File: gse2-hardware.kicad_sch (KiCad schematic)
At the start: 66 parts, among them J1 PJ-002A, J16 ARM, J17 ALARM, J2 PJ-002A, J3 ARM Cortex Debug, J33 AI_Ports, J34 Misc_Ports, J4 USB-C, Q1 DMP3099L, Q15 DMG3402L, U27 USBLC6-2SC6, Y1 16MHz

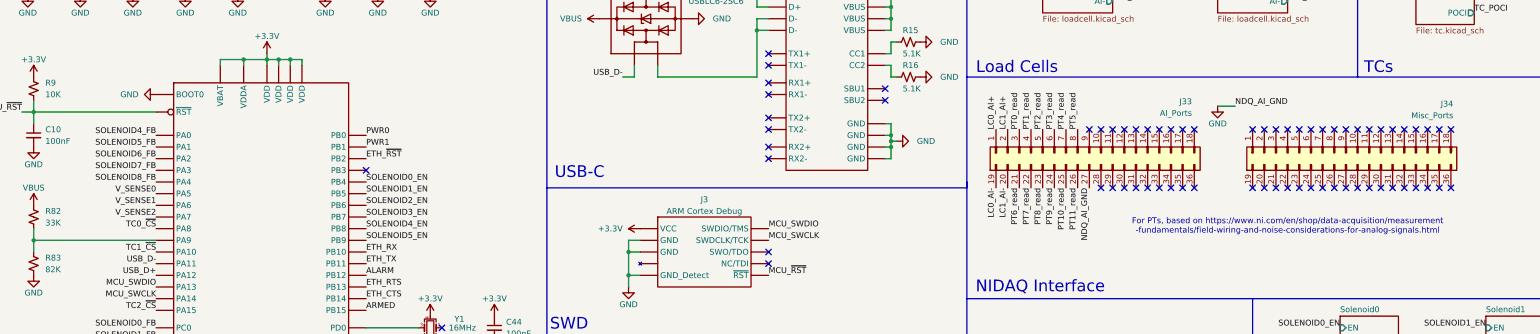
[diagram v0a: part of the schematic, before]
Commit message: Layed out (no edge cuts)g
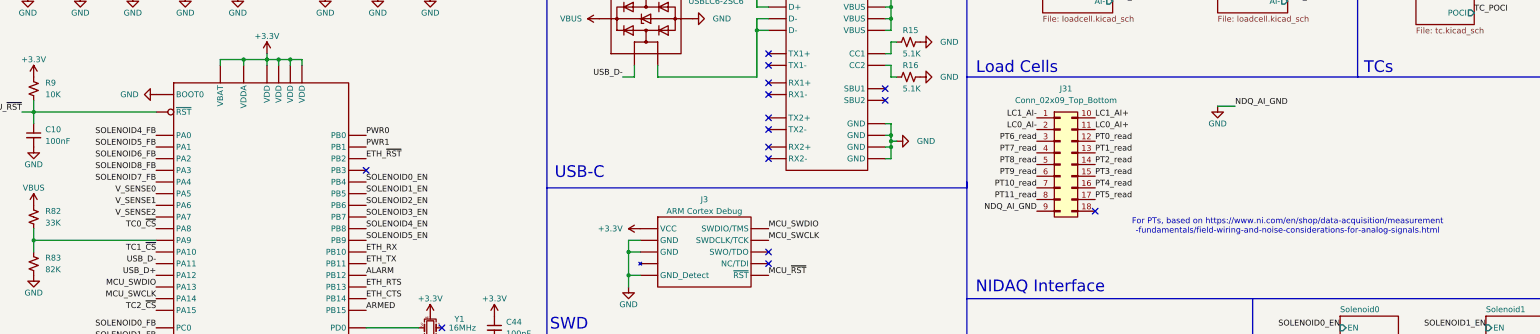
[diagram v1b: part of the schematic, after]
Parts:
- removed J33: AI_Ports, symbol Connector_Generic:Conn_02x18_Top_Bottom
- removed J34: Misc_Ports, symbol Connector_Generic:Conn_02x18_Top_Bottom
- added J31: Conn_02x09_Top_Bottom, 0UCIRP-KiCAD-Lib:2x9_MOLEX, symbol Connector_Generic:Conn_02x09_Top_Bottom
- J17: footprint TerminalBlock_MetzConnect:TerminalBlock_MetzConnect_Type055_RT01502HDWU_1x02_P5.00mm_Horizontal -> 0UCIRP-KiCAD-Lib:GX-16 2 pin
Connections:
- net GND: now also J31.9 (Pin_9)
- net LC0_AI+: now also J31.11 (Pin_11)
- net LC0_AI-: now also J31.2 (Pin_2)
- net LC1_AI+: now also J31.10 (Pin_10)
- net LC1_AI-: now also J31.1 (Pin_1)
- net PT0_read: now also J31.12 (Pin_12)
- net PT10_read: now also J31.7 (Pin_7)
- net PT11_read: now also J31.8 (Pin_8)
- net PT1_read: now also J31.13 (Pin_13)
- net PT2_read: now also J31.14 (Pin_14)
- net PT3_read: now also J31.15 (Pin_15)
- net PT4_read: now also J31.16 (Pin_16)
- net PT5_read: now also J31.17 (Pin_17)
- net PT6_read: now also J31.3 (Pin_3)
- net PT7_read: now also J31.4 (Pin_4)
- net PT8_read: now also J31.5 (Pin_5)
- net PT9_read: now also J31.6 (Pin_6)
- net SOLENOID7_FB: now also U2.20 (PA4); no longer U2.17 (PA3)
- net SOLENOID8_FB: now also U2.17 (PA3); no longer U2.20 (PA4)
- no-connect marks 73 -> 19

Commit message: Fixed updates form last night not pushing
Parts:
- added H1, H2, H3, H4: MountingHole_Pad, MountingHole:MountingHole_4.3mm_M4_Pad_Via, symbol Mechanical:MountingHole_Pad
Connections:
- net at D1.2 (A), J1.1, R2.2: now also R10.2
- net at D4.2 (A), J2.1, R7.2: now also R8.2
- net at D1.1 (K), D4.1 (K), F1.1: no longer R10.2, R8.2
- no-connect marks 19 -> 23
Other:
- moved on the sheet: D1, D4, D5, D6, R10, R8

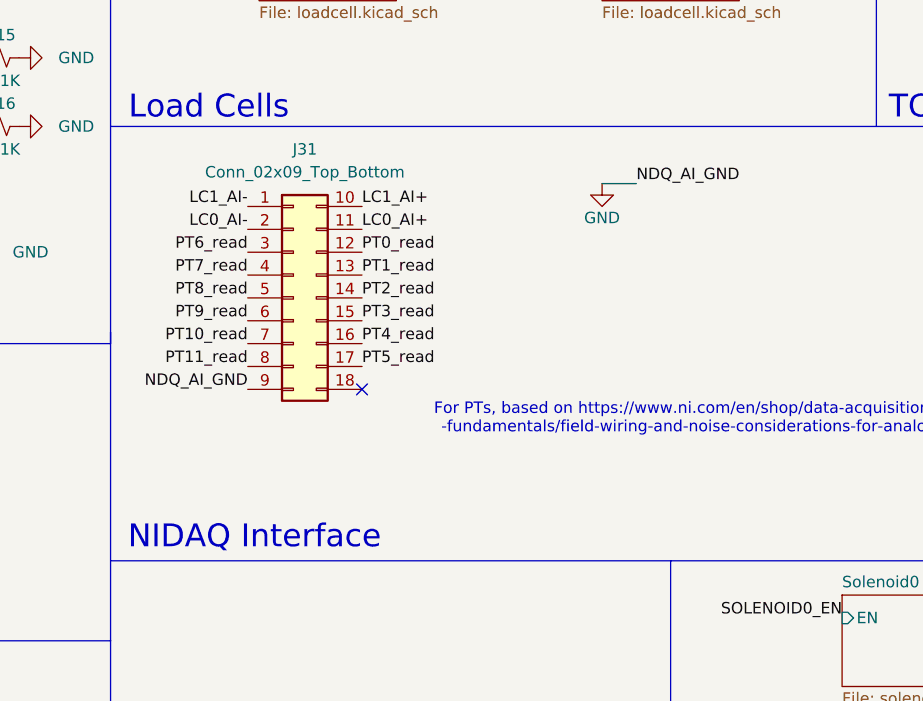
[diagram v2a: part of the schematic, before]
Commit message: Fixed connectors
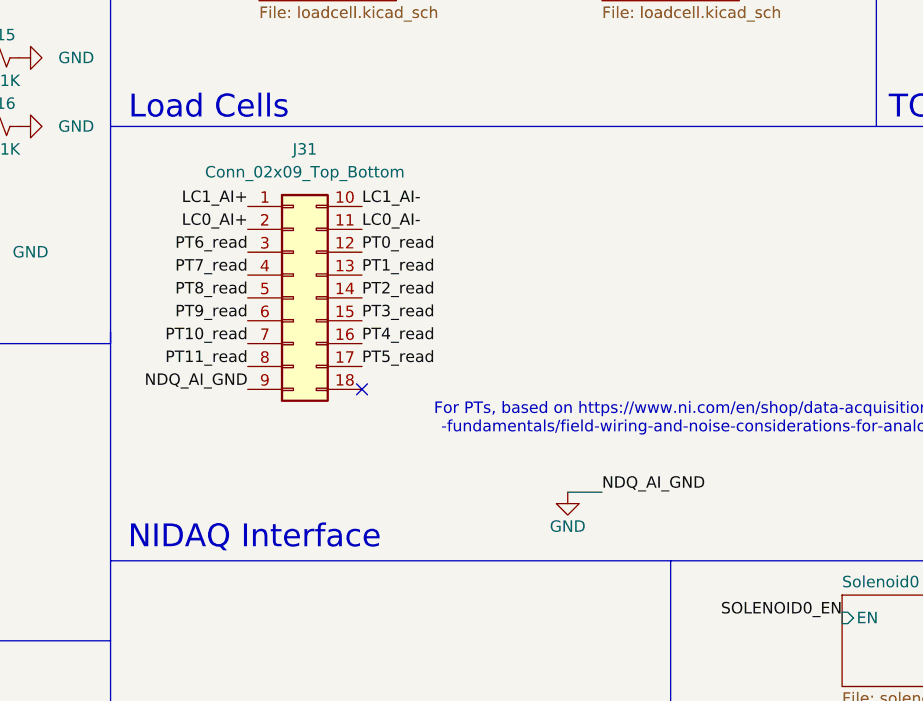
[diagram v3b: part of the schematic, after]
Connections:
- net LC0_AI+: now also J31.2 (Pin_2); no longer J31.11 (Pin_11)
- net LC0_AI-: now also J31.11 (Pin_11); no longer J31.2 (Pin_2)
- net LC1_AI+: now also J31.1 (Pin_1); no longer J31.10 (Pin_10)
- net LC1_AI-: now also J31.10 (Pin_10); no longer J31.1 (Pin_1)
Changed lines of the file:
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@@
 	(wire
 		(pts
-			(xy 287.02 48.26) (xy 290.83 48.26)
+			(xy 283.21 82.55) (xy 287.02 82.55)
 		)
 		(stroke
@@
 		)
 	)
+	(label "LC0_AI+"
+		(at 247.65 53.34 180)
+		(effects
+			(font
+				(size 1.27 1.27)
+			)
+			(justify right bottom)
+		)
+	)
 	(label "SOLENOID0_FB"
 		(at 326.39 101.6 0)
@@
 		)
 	)
-	(label "LC0_AI-"
-		(at 247.65 53.34 180)
-		(effects
-			(font
-				(size 1.27 1.27)
-			)
-			(justify right bottom)
-		)
-	)
 	(label "MCU_SWCLK"
 		(at 189.23 77.47 0)
@@
 		)
 	)
+	(label "LC0_AI-"
+		(at 260.35 53.34 0)
+		(effects
+			(font
+				(size 1.27 1.27)
+			)
+			(justify left bottom)
+		)
+	)
 	(label "EMATCH1_FIRE"
 		(at 55.88 116.84 180)
@@
 		)
 	)
+	(label "LC1_AI-"
+		(at 260.35 50.8 0)
+		(effects
+			(font
+				(size 1.27 1.27)
+			)
+			(justify left bottom)
+		)
+	)
 	(label "SOLENOID4_EN"
 		(at 101.6 74.93 0)
@@
 	)
 	(label "NDQ_AI_GND"
-		(at 290.83 48.26 0)
+		(at 287.02 82.55 0)
 		(effects
 			(font
@@
 		)
 	)
+	(label "LC1_AI+"
+		(at 247.65 50.8 180)
+		(effects
+			(font
+				(size 1.27 1.27)
+			)
+			(justify right bottom)
+		)
+	)
 	(label "TC_SCK"
 		(at 358.14 24.13 180)
@@
 		)
 	)
-	(label "LC1_AI-"
-		(at 247.65 50.8 180)
-		(effects
-			(font
-				(size 1.27 1.27)
-			)
-			(justify right bottom)
-		)
-	)
 	(label "SOLENOID5_FB"
 		(at 55.88 57.15 180)
@@
 		)
 	)
-	(label "LC0_AI+"
-		(at 260.35 53.34 0)
-		(effects
-			(font
-				(size 1.27 1.27)
-			)
-			(justify left bottom)
-		)
-	)
 	(label "PT0_read"
 		(at 26.67 161.29 0)
@@
 		)
 	)
-	(label "LC1_AI+"
-		(at 260.35 50.8 0)
-		(effects
-			(font
-				(size 1.27 1.27)
-			)
-			(justify left bottom)
-		)
-	)
 	(label "PT0_read"
 		(at 260.35 55.88 0)
@@
 	(symbol
 		(lib_id "power:GND")
-		(at 287.02 48.26 0)
+		(at 283.21 82.55 0)
 		(unit 1)
 		(exclude_from_sim no)
@@
 		(dnp no)
 		(property "Reference" "#PWR03"
-			(at 287.02 54.61 0)
+			(at 283.21 88.9 0)
 			(effects
 				(font
@@
 		)
 		(property "Value" "GND"
-			(at 287.02 52.07 0)
+			(at 283.21 86.36 0)
 			(effects
 				(font
@@
 		)
 		(property "Footprint" ""
-			(at 287.02 48.26 0)
+			(at 283.21 82.55 0)
 			(effects
 				(font
@@
 		)
 		(property "Datasheet" ""
-			(at 287.02 48.26 0)
+			(at 283.21 82.55 0)
 			(effects
 				(font
@@
 		)
 		(property "Description" ""
-			(at 287.02 48.26 0)
+			(at 283.21 82.55 0)
 			(effects
 				(font

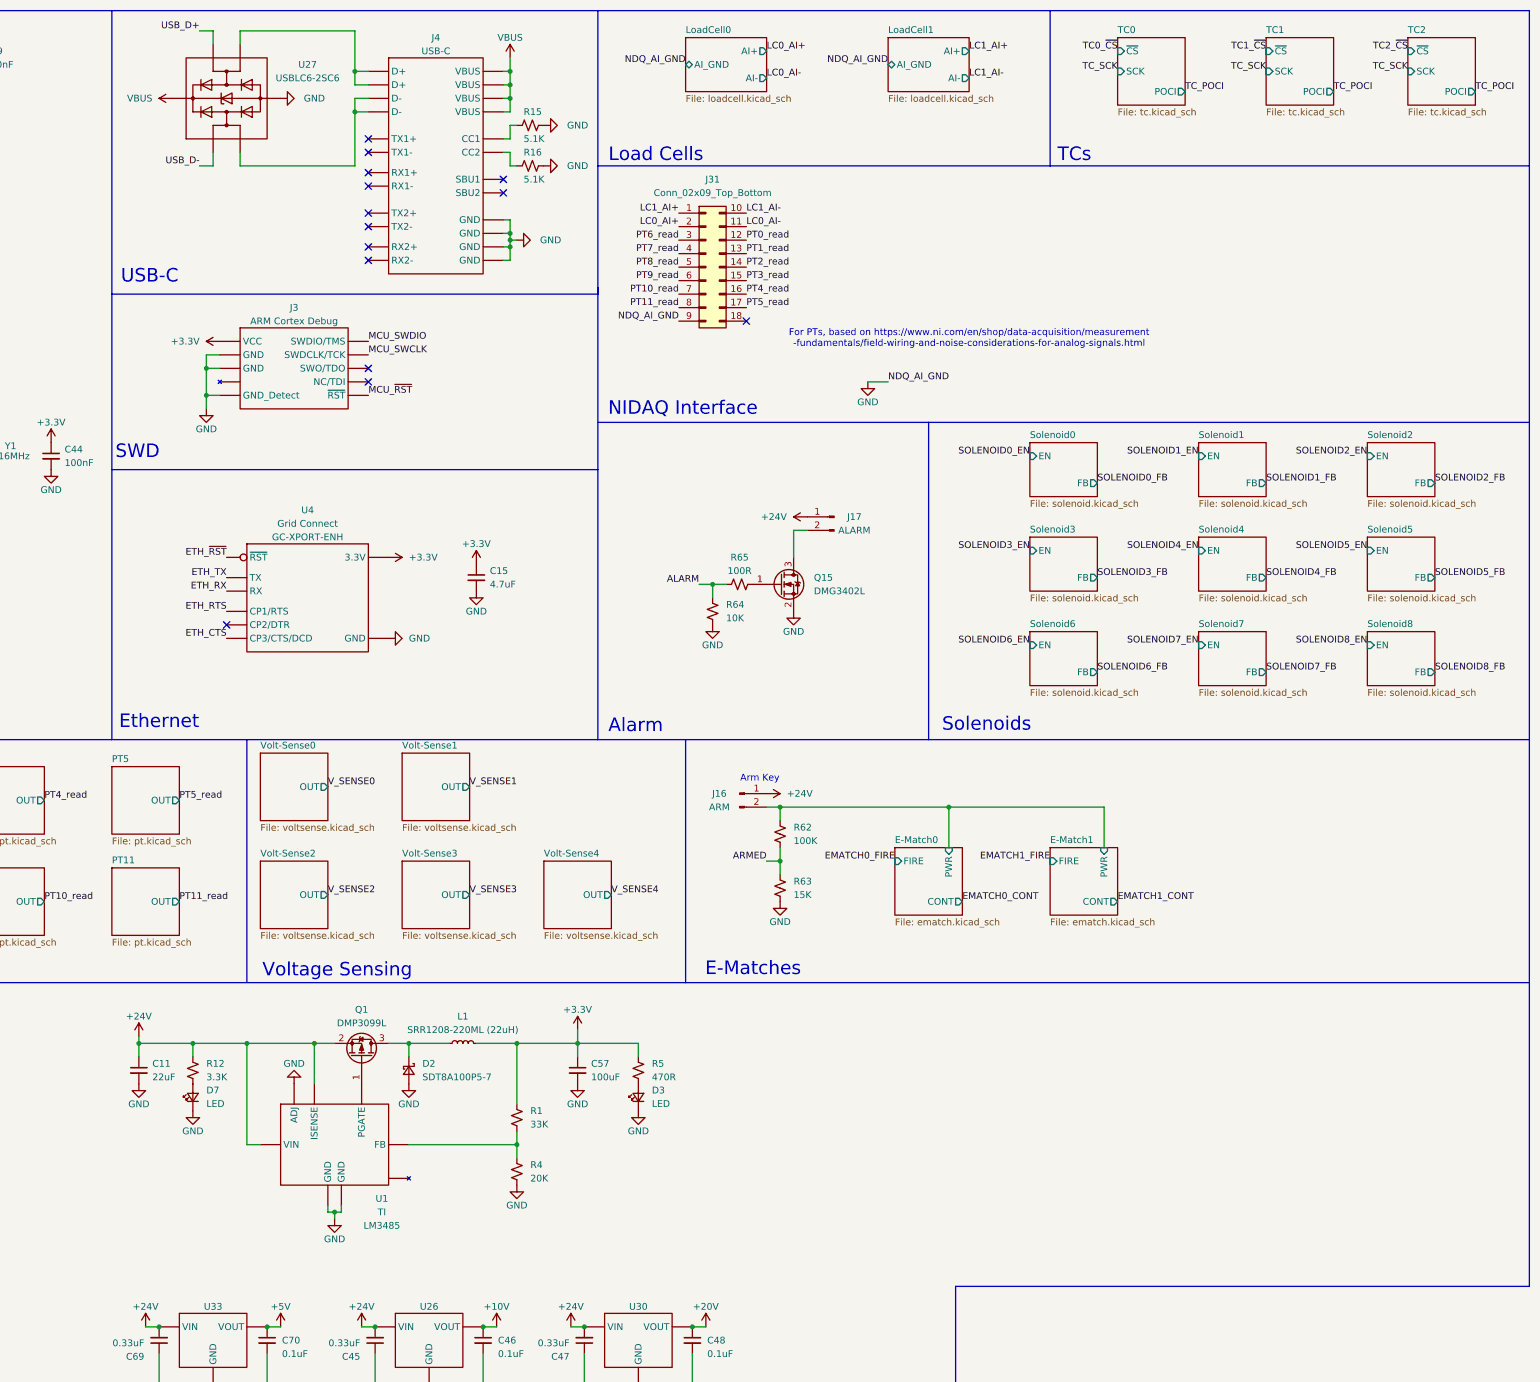
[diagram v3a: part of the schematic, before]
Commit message: Ready to order besides BOM. I might mess w/ silkscreen more. 3v3 reg changed
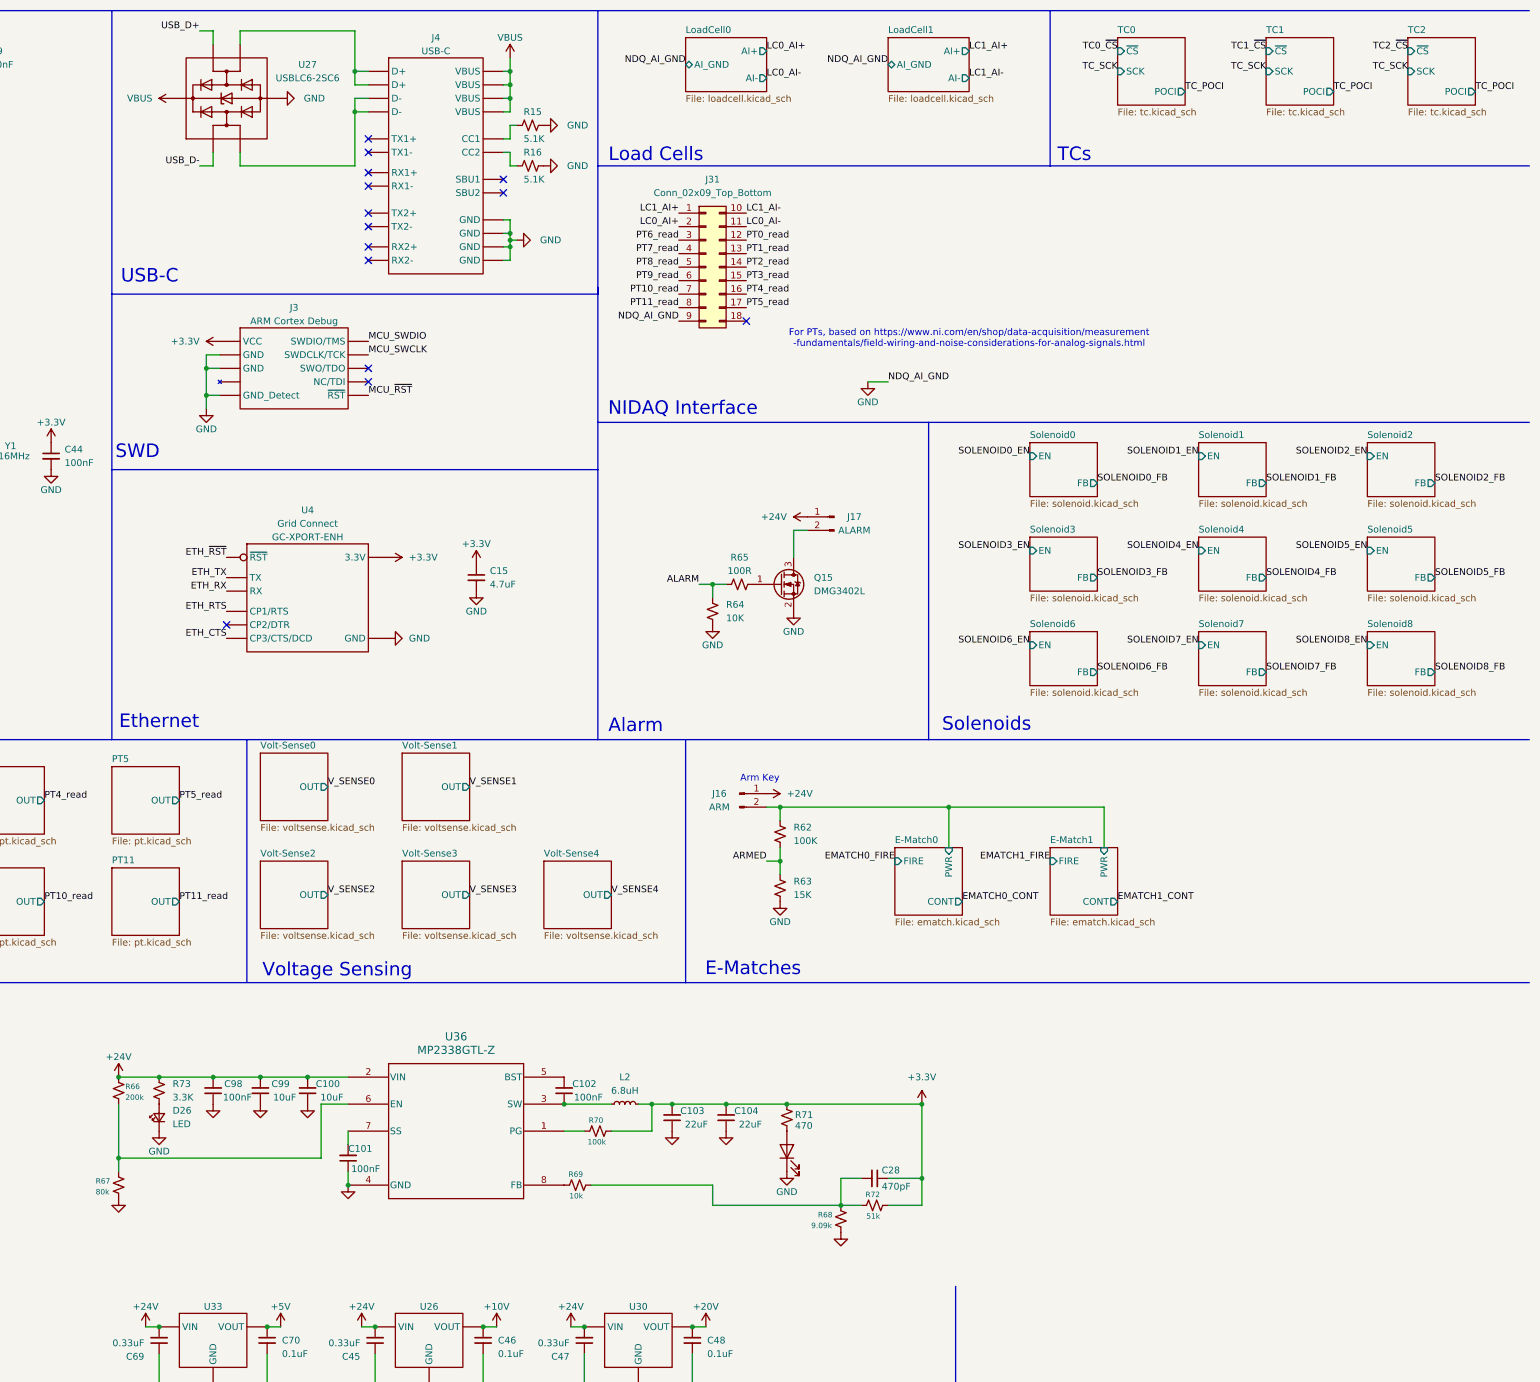
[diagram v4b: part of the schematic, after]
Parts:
- removed C11: 22uF, Capacitor_SMD:C_0603_1608Metric, symbol Device:C_Small
- removed C57: 100uF, Capacitor_SMD:C_0603_1608Metric, symbol Device:C_Small
- removed D2: SDT8A100P5-7, Diode_SMD:D_PowerDI-5, symbol Device:D_Schottky_Small
- removed D3, D7: LED, LED_SMD:LED_0603_1608Metric, symbol Device:LED_Small
- removed L1: SRR1208-220ML (22uH), Inductor_SMD:L_Bourns_SRR1208_12.7x12.7mm, symbol Device:L_Small
- removed Q1: DMP3099L, Package_TO_SOT_SMD:SOT-23-3, symbol Device:Q_PMOS_GSD
- removed R1: 33K, Resistor_SMD:R_0603_1608Metric, symbol Device:R_Small_US
- removed R12: 3.3K, Resistor_SMD:R_0603_1608Metric, symbol Device:R_Small_US
- removed R4: 20K, Resistor_SMD:R_0603_1608Metric, symbol Device:R_Small_US
- removed R5: 470R, Resistor_SMD:R_0603_1608Metric, symbol Device:R_Small_US
- removed U1: ~, Package_SO:VSSOP-8_3x3mm_P0.65mm, symbol UCIRP-KiCAD-Lib:LM3485
- added C100, C99: 10uF, Capacitor_SMD:C_0603_1608Metric, symbol Device:C_Small
- added C101, C102, C98: 100nF, Capacitor_SMD:C_0603_1608Metric, symbol Device:C_Small
- added C103, C104: 22uF, Capacitor_SMD:C_0603_1608Metric, symbol Device:C_Small
- added C28: 470pF, Capacitor_SMD:C_0603_1608Metric, symbol Device:C_Small
- added D26: LED, LED_SMD:LED_0603_1608Metric, symbol Device:LED_Small
- added D42: BLUE_LED, Diode_SMD:D_0603_1608Metric, symbol Device:LED
- added L2: 6.8uH, 0UCIRP-KiCAD-Lib:IND_VLS6045EX-6R8M, symbol Device:L_Small
- added R66: 200k, Resistor_SMD:R_0603_1608Metric, symbol Device:R_Small_US
- added R67: 80k, Resistor_SMD:R_0603_1608Metric, symbol Device:R_Small_US
- added R68: 9.09k, Resistor_SMD:R_0603_1608Metric, symbol Device:R_Small_US
- added R69: 10k, Resistor_SMD:R_0603_1608Metric, symbol Device:R_Small_US
- added R70: 100k, Resistor_SMD:R_0603_1608Metric, symbol Device:R_Small_US
- added R71: 470, Resistor_SMD:R_0603_1608Metric, symbol Device:R_Small_US
- added R72: 51k, Resistor_SMD:R_0603_1608Metric, symbol Device:R_Small_US
- added R73: 3.3K, Resistor_SMD:R_0603_1608Metric, symbol Device:R_Small_US
- added U36: MP2338GTL-Z, SOT583_MP2338_MNP, symbol UCIRP-KiCAD-Lib:MP2338GTL-Z
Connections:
- net +24V: now also C100.2, C98.2, C99.2, R66.1, R73.2, U36.2 (VIN)
- net +3.3V: now also C103.2, C104.2, C28.1, L2.2, R70.2, R71.1, R72.2
- net GND: now also C100.1, C101.1, C103.1, C104.1, C98.1, C99.1, D26.1 (K), D42.1 (K), R67.2, R68.2, U36.4 (GND)
- new net: C28.2, R68.1, R69.2, R72.1
- new net: R69.1, U36.8 (FB)
- new net: C101.2, U36.7 (SS)
- new net: D26.2 (A), R73.1
- new net: R66.2, R67.1, U36.6 (EN)
- new net: R70.1, U36.1 (PG)
- new net: C102.1, L2.1, U36.3 (SW)
- new net: C102.2, U36.5 (BST)
- new net: D42.2 (A), R71.2
